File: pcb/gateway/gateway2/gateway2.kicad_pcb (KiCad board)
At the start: 4 copper layers, 77 x 47 mm, 119 parts, among them J1 Conn_ARM_JTAG_SWD_10, J10 Conn_01x07, J2 RJ45_Kycon_G7LX-A88S7-BP-GY, J8 Conn_01x07, J9 Conn_01x07, P1 USB_C_Plug_USB2.0, SW1 RST, SW2 BOOT, U1 RP2354B, U10 74AHC125, U2 W6300-Q, U3 RT6150AGQW, U8 74AHC125, U9 74AHC125, Y1 ABM8-272-T3, Y2 25MHz

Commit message: WIP.
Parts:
- removed C43, C44: 100n, Capacitor_SMD:C_0603_1608Metric
- removed CP6, CP7: C_Array_4x0612, AVX_Capacitor_Array:C_Array_4x0612
- removed J10, J9: Conn_01x07, Connector_JST:JST_GH_BM07B-GHS-TBT_1x07-1MP_P1.25mm_Vertical
- removed JP11, JP13: SolderJumper_2_Open, Jumper:SolderJumper-2_P1.3mm_Open_RoundedPad1.0x1.5mm
- removed JP12, JP14: SolderJumper_2_Bridged, Jumper:SolderJumper-2_P1.3mm_Bridged_RoundedPad1.0x1.5mm
- removed L6: AOTA-B201610S3R3-101-T, Abracon_AOTA_B201610S:L_0806_2016Metric
- removed R36, R39: 100k, Resistor_SMD:R_0603_1608Metric
- removed R37, R40: 10k, Resistor_SMD:R_0603_1608Metric
- removed RN6, RN7: R_Pack04, Resistor_SMD:R_Array_Concave_4x0603
- removed U10, U9: 74AHC125, Package_DFN_QFN:DHVQFN-14-1EP_2.5x3mm_P0.5mm_EP1x1.5mm
- added L1: L, Inductor_SMD:L_Abracon_AOTA-B201610S, F.Cu at (145.7, 70.2)
- U2: footprint WIZnet_W6300:W6300-Q -> Package_QFP:LQFP-48-1EP_7x7mm_P0.5mm_EP3.6x3.6mm_ThermalVias
- moved R11 108.0 mm to (100.9, 68.7)
- moved R10 104.2 mm to (100.5, 91.2)
- moved C30 94.3 mm to (107.0, 92.8)
- moved L4 92.1 mm to (111.8, 99.2)
- moved C23 91.8 mm to (108.1, 99.2)
- moved C22 88.6 mm to (111.3, 93.8)
- moved C17 87.5 mm to (108.5, 96.2)
- moved R19 86.8 mm to (121.2, 98.8)
- moved R18 86.8 mm to (121.2, 97.0)
- moved R23 84.0 mm to (160.6, 59.0)
- moved R24 81.5 mm to (163.6, 60.4)
- moved R21 80.3 mm to (170.5, 65.7)
- moved R22 78.2 mm to (164.1, 63.3)
- moved R20 76.7 mm to (169.7, 69.1)
- moved R25 76.2 mm to (162.3, 69.3)
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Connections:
- net Net-(P1-D+-PadA6) renamed /USB_D+
- net Net-(P1-D--PadA7) renamed /USB_D-
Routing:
- net +1V1: track 15.0 -> 29.0 mm, vias 3 -> 9
- net /USB_D+: track 0.00 -> 8.34 mm
- net /USB_D-: track 0.00 -> 7.97 mm
- net Net-(U1-VREG_AVDD): track 0.00 -> 5.84 mm
- net Net-(U1-USB_DM): track 4.50 -> 8.23 mm
- net Net-(U1-SWCLK): track 0.00 -> 2.61 mm
- net Net-(U1-SWDIO): track 0.00 -> 1.91 mm
- net GND: track 15.1 -> 14.5 mm, vias 25 -> 26
- net +3V3: track 17.4 -> 17.8 mm, vias 3 -> 4

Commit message: Moving stuff to proper library.
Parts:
- L1: value L -> 3.3µ
- SW1, SW2: footprint Littelfuse_CK_PTS815:SW_SPST_CK_PTS815_Sx250SMTR_LFS -> Button_Switch_SMD:SW_SPST_CK_PTS815_Sx250SMTR_LFS
- U3: footprint Richtek_RT6150:WDFN-10-1EP_3x3mm_P0.5mm_EP1.8x2.5mm -> Package_DFN_QFN:WDFN-10-1EP_3x3mm_P0.5mm_EP1.8x2.5mm
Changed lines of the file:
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@@
 		(tags "capacitor")
 		(property "Reference" "C42"
-			(at 0 -1.43 0)
+			(at -0.05 1.5 0)
 			(layer "F.SilkS")
 			(effects
@@
 		(tags "DHVQFN NoLead")
 		(property "Reference" "U8"
-			(at 0 -2.8 0)
+			(at 2.7 2.2875 0)
 			(layer "F.SilkS")
 			(effects
@@
 			)
 		)
-		(model "${KIPRJMOD}/Models/74AHC125BQ,115.stp"
-			(offset
-				(xyz 0 0 0)
-			)
-			(scale
-				(xyz 1 1 1)
-			)
-			(rotate
-				(xyz -0 -0 -0)
-			)
-		)
 	)
 	(footprint "Resistor_SMD:R_0603_1608Metric"
@@
 		)
 	)
-	(footprint "Littelfuse_CK_PTS815:SW_SPST_CK_PTS815_Sx250SMTR_LFS"
+	(footprint "Button_Switch_SMD:SW_SPST_CK_PTS815_Sx250SMTR_LFS"
 		(layer "F.Cu")
 		(at 148.3 60.55)
@@
 			)
 		)
-		(pad "1" smd rect
+		(pad "1" smd roundrect
 			(at -2.25 -1.075)
 			(size 1 0.7)
 			(layers "F.Cu" "F.Mask" "F.Paste")
+			(roundrect_rratio 0.25)
 			(net "GND")
 			(pinfunction "1_1")
 			(pintype "passive")
 		)
-		(pad "1" smd rect
+		(pad "1" smd roundrect
 			(at 2.25 -1.075)
 			(size 1 0.7)
 			(layers "F.Cu" "F.Mask" "F.Paste")
+			(roundrect_rratio 0.25)
 			(net "GND")
 			(pinfunction "1_1")
@@
 		)
 		(embedded_fonts no)
-		(model "${KIPRJMOD}/Littelfuse_CK_PTS815_KiCad_Library/Littelfuse_CK_PTS815.3dshapes/SW_SPST_CK_PTS815_Sx250SMTR_LFS.step"
+		(model "${KICAD10_3DMODEL_DIR}/Button_Switch_SMD.3dshapes/SW_SPST_CK_PTS815_Sx250SMTR_LFS.step"
 			(offset
 				(xyz 0 0 0)
@@
 			)
 		)
-		(model "${KIPRJMOD}/Models/RJ45_Kycon_G7LX-A88S7-BP-GY_Horizontal.wrl"
-			(offset
-				(xyz 0 0 0)
-			)
-			(scale
-				(xyz 1 1 1)
-			)
-			(rotate
-				(xyz 0 0 0)
-			)
-		)
 	)
-	(footprint "Richtek_RT6150:WDFN-10-1EP_3x3mm_P0.5mm_EP1.8x2.5mm"
+	(footprint "Package_DFN_QFN:WDFN-10-1EP_3x3mm_P0.5mm_EP1.8x2.5mm"
 		(layer "F.Cu")
 		(at 159.025 66.1)
-		(descr "Richtek RT6150AGQW, WDFN-10L 3x3mm P0.5mm, exposed-pad land pattern 1.8x2.5mm; copied from KiCad stock WDFN-10 footprint")
+		(descr "WDFN, 10 Pin (https://www.onsemi.com/pdf/datasheet/nis5420-d.pdf)")
 		(tags "WDFN NoLead")
 		(property "Reference" "U3"
-			(at 3.175 -0.7 0)
+			(at 0 -2.45 0)
 			(layer "F.SilkS")
 			(effects
@@
 			(unit
 				(name "A")
-				(pins "6" "7" "8" "3" "9" "5" "11" "1" "10" "2" "4")
+				(pins "8" "5" "6" "7" "3" "9" "11" "1" "10" "2" "4")
 			)
 		)
@@
 		)
 		(embedded_fonts no)
-		(model "${KIPRJMOD}/Richtek_RT6150_KiCad_Library/Richtek_RT6150.3dshapes/DFN-10-1EP_3x3mm_P0.5mm_EP1.65x2.38mm.step"
+		(model "${KICAD10_3DMODEL_DIR}/Package_DFN_QFN.3dshapes/WDFN-10-1EP_3x3mm_P0.5mm_EP1.8x2.5mm.step"
 			(offset
 				(xyz 0 0 0)
@@
 		)
 		(embedded_fonts no)
-		(model "${KIPRJMOD}/Models/CA064X104M8RACTU.step"
-			(offset
-				(xyz 1.5 0.8 0)
-			)
-			(scale
-				(xyz 1 1 0.8)
-			)
-			(rotate
-				(xyz -0 -0 -90)
-			)
-		)
 	)
 	(footprint "Capacitor_SMD:C_0603_1608Metric"
@@
 			)
 		)
-		(property "Value" "L"
+		(property "Value" "3.3µ"
 			(at 0 1.55 0)
 			(layer "F.Fab")
@@
 		)
 	)
-	(footprint "Littelfuse_CK_PTS815:SW_SPST_CK_PTS815_Sx250SMTR_LFS"
+	(footprint "Button_Switch_SMD:SW_SPST_CK_PTS815_Sx250SMTR_LFS"
 		(layer "F.Cu")
 		(at 134.475 60.1)
@@
 			)
 		)
-		(pad "1" smd rect
+		(pad "1" smd roundrect
 			(at -2.25 -1.075)
 			(size 1 0.7)
 			(layers "F.Cu" "F.Mask" "F.Paste")
+			(roundrect_rratio 0.25)
 			(net "GND")
 			(pinfunction "1_1")
 			(pintype "passive")
 		)
-		(pad "1" smd rect
+		(pad "1" smd roundrect
 			(at 2.25 -1.075)
 			(size 1 0.7)
 			(layers "F.Cu" "F.Mask" "F.Paste")
+			(roundrect_rratio 0.25)
 			(net "GND")
 			(pinfunction "1_1")
@@
 		)
 		(embedded_fonts no)
-		(model "${KIPRJMOD}/Littelfuse_CK_PTS815_KiCad_Library/Littelfuse_CK_PTS815.3dshapes/SW_SPST_CK_PTS815_Sx250SMTR_LFS.step"
+		(model "${KICAD10_3DMODEL_DIR}/Button_Switch_SMD.3dshapes/SW_SPST_CK_PTS815_Sx250SMTR_LFS.step"
 			(offset
 				(xyz 0 0 0)

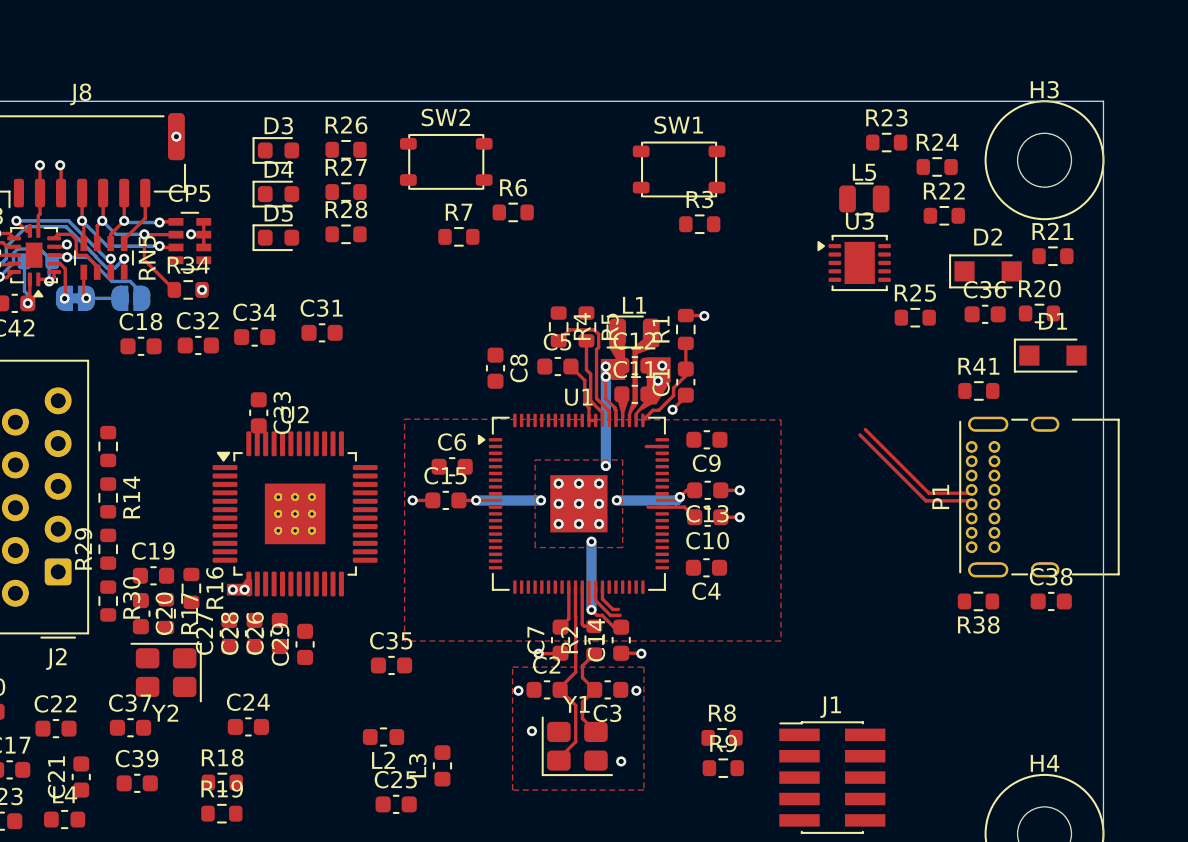
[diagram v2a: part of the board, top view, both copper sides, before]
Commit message: Working on power converter.
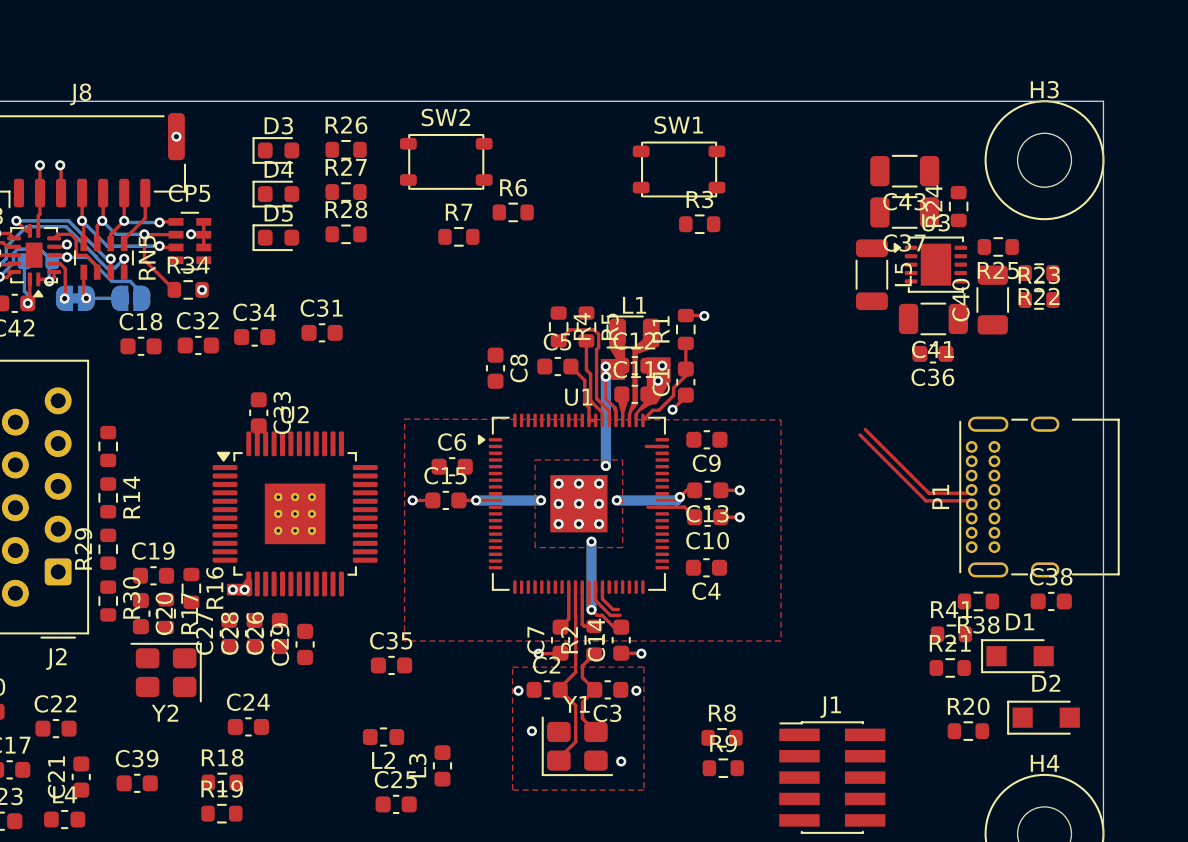
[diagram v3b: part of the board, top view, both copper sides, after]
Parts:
- added C40: 22μ/6.3V, Capacitor_SMD:C_1206_3216Metric, F.Cu at (166.9, 68.3)
- added C41: 22μ/6.3V, Capacitor_SMD:C_1206_3216Metric, F.Cu at (163.4, 69.4)
- added C43: 22μ/6.3V, Capacitor_SMD:C_1206_3216Metric, F.Cu at (161.7, 60.6)
- C37: value 47μ/6.3V -> 22μ/6.3V; footprint Capacitor_SMD:C_0603_1608Metric -> Capacitor_SMD:C_1206_3216Metric
- L5: footprint Abracon_AOTA_B201610S:L_0806_2016Metric -> Inductor_SMD:L_1206_3216Metric
- moved C37 55.2 mm to (161.7, 63.1), turned to 180 degrees
- moved D2 26.7 mm to (170.1, 93.1)
- moved R21 25.2 mm to (164.4, 90.2)
- moved R20 25.2 mm to (165.5, 93.9)
- moved D1 18.0 mm to (168.6, 89.5)
- moved R41 14.5 mm to (164.5, 88.2)
- moved R23 13.0 mm to (169.7, 68.3)
- moved R22 6.57 mm to (169.7, 66.7), turned to 180 degrees
- moved R25 6.47 mm to (167.2, 65.2), turned to 180 degrees
- moved U3 4.53 mm to (163.6, 66.2)
- moved L5 4.52 mm to (159.8, 66.8), turned to -90 degrees
- moved C36 3.89 mm to (163.4, 71.5), turned to 180 degrees
- moved R24 2.67 mm to (164.9, 62.8), turned to 90 degrees

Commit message: Power converter routed.
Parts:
- moved D1 17.9 mm to (160.5, 73.5), turned to -90 degrees
- moved R9 8.81 mm to (148.6, 87.6)
- moved J1 7.29 mm to (159.2, 89.6)
- moved R20 6.96 mm to (164.6, 87.0), turned to -90 degrees
- moved R8 5.57 mm to (148.6, 89.2), turned to 180 degrees
- moved R41 5.06 mm to (169.4, 87.0), turned to 90 degrees
- moved R21 3.63 mm to (166.2, 87.0), turned to -90 degrees
- moved C41 3.62 mm to (162.8, 73.0), turned to 90 degrees
- moved C43 3.56 mm to (164.0, 63.4)
- moved C37 3.54 mm to (164.0, 65.8)
- moved R24 3.48 mm to (167.2, 65.4)
- moved C40 2.68 mm to (167.6, 70.9)
- moved R23 2.68 mm to (170.3, 70.9)
- moved R25 2.68 mm to (167.9, 67.8)
- moved R22 2.68 mm to (170.3, 69.3), turned to 0 degrees
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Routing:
- net /Power/V_USB: track 0.00 -> 22.1 mm, vias 0 -> 1
- net GNDPWR: track 0.00 -> 19.9 mm
- net GND: track 14.5 -> 26.5 mm, vias 26 -> 40
- net Net-(P1-CC2): track 0.00 -> 8.98 mm, vias 0 -> 1
- net Net-(U3-EN): track 0.00 -> 8.32 mm, vias 0 -> 2
- net POWER_SAVE: track 0.00 -> 7.09 mm, vias 0 -> 2
- net Net-(P1-CC1): track 0.00 -> 6.88 mm
- net +3V3: track 17.8 -> 23.2 mm, vias 4 -> 9
- net +5V: track 0.00 -> 4.60 mm
- net Net-(U1-SWCLK): track 2.61 -> 6.49 mm
- net Net-(U1-SWDIO): track 1.91 -> 5.37 mm
- net /USB_D-: track 7.97 -> 11.1 mm
- net /USB_D+: track 8.34 -> 11.4 mm
- net Net-(U3-FB): track 0.00 -> 2.98 mm
- net VBUS_MONITOR: track 0.00 -> 2.31 mm

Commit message: Lookinmg where to place the buttons at.
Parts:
- moved SW2 31.1 mm to (160.0, 77.8)
- moved R7 24.9 mm to (154.6, 80.2)
- moved SW1 24.6 mm to (160.0, 82.2), turned to 180 degrees
- moved R6 22.2 mm to (154.6, 78.4)
- moved R3 21.3 mm to (154.8, 84.4), turned to 180 degrees
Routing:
- net /USB_D+: track 11.4 -> 1.70 mm
- net Net-(U1-RUN): track 0.00 -> 9.29 mm
- net /USB_D-: track 11.1 -> 2.03 mm
- net /Power/V_USB: track 22.1 -> 23.3 mm
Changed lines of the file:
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@@
 	(footprint "Resistor_SMD:R_0603_1608Metric"
 		(layer "F.Cu")
-		(at 138.45 63.1)
+		(at 154.6 78.4)
 		(descr "Resistor SMD 0603 (1608 Metric), square (rectangular) end terminal, IPC-7351 nominal, (Body size source: IPC-SM-782 page 72, https://www.pcb-3d.com/wordpress/wp-content/uploads/ipc-sm-782a_amendment_1_and_2.pdf)")
 		(tags "resistor")
@@
 	(footprint "Button_Switch_SMD:SW_SPST_CK_PTS815_Sx250SMTR_LFS"
 		(layer "F.Cu")
-		(at 148.3 60.55)
+		(at 160 82.2 180)
 		(descr "C&K / Littelfuse PTS815 series microminiature SMT top-actuated tactile switch, 4.2 x 3.2 mm, 2.5 mm height")
 		(tags "C&K Littelfuse PTS815 tactile SPST NO switch")
@@
 		(duplicate_pad_numbers_are_jumpers no)
 		(fp_line
-			(start -2.2 -1.6)
-			(end -2.2 -1.45)
+			(start 2.2 1.45)
+			(end 2.2 1.6)
 			(stroke
 				(width 0.12)
@@
 		)
 		(fp_line
-			(start -2.2 -0.7)
-			(end -2.2 0.7)
+			(start 2.2 -0.7)
+			(end 2.2 0.7)
 			(stroke
 				(width 0.12)
@@
 		)
 		(fp_line
-			(start -2.2 1.45)
-			(end -2.2 1.6)
+			(start 2.2 -1.6)
+			(end 2.2 -1.45)
 			(stroke
 				(width 0.12)
@@
 		)
 		(fp_line
-			(start -2.1 -1.6)
-			(end 2.1 -1.6)
+			(start -2.1 1.6)
+			(end 2.1 1.6)
 			(stroke
 				(width 0.12)
@@
 		)
 		(fp_line
-			(start -2.1 1.6)
-			(end 2.1 1.6)
+			(start -2.1 -1.6)
+			(end 2.1 -1.6)
 			(stroke
 				(width 0.12)
@@
 		)
 		(fp_line
-			(start 2.2 -1.6)
-			(end 2.2 -1.45)
+			(start -2.2 1.45)
+			(end -2.2 1.6)
 			(stroke
 				(width 0.12)
@@
 		)
 		(fp_line
-			(start 2.2 -0.7)
-			(end 2.2 0.7)
+			(start -2.2 -0.7)
+			(end -2.2 0.7)
 			(stroke
 				(width 0.12)
@@
 		)
 		(fp_line
-			(start 2.2 1.45)
-			(end 2.2 1.6)
+			(start -2.2 -1.6)
+			(end -2.2 -1.45)
 			(stroke
 				(width 0.12)
@@
 		)
 		(pad "1" smd roundrect
-			(at -2.25 -1.075)
+			(at -2.25 -1.075 180)
 			(size 1 0.7)
 			(layers "F.Cu" "F.Mask" "F.Paste")
@@
 		)
 		(pad "1" smd roundrect
-			(at 2.25 -1.075)
+			(at 2.25 -1.075 180)
 			(size 1 0.7)
 			(layers "F.Cu" "F.Mask" "F.Paste")
@@
 		)
 		(pad "2" smd roundrect
-			(at -2.25 1.075)
+			(at -2.25 1.075 180)
 			(size 1 0.7)
 			(layers "F.Cu" "F.Mask" "F.Paste")
@@
 		)
 		(pad "2" smd roundrect
-			(at 2.25 1.075)
+			(at 2.25 1.075 180)
 			(size 1 0.7)
 			(layers "F.Cu" "F.Mask" "F.Paste")
@@
 	(footprint "Resistor_SMD:R_0603_1608Metric"
 		(layer "F.Cu")
-		(at 149.525 63.8)
+		(at 154.825 84.4 180)
 		(descr "Resistor SMD 0603 (1608 Metric), square (rectangular) end terminal, IPC-7351 nominal, (Body size source: IPC-SM-782 page 72, https://www.pcb-3d.com/wordpress/wp-content/uploads/ipc-sm-782a_amendment_1_and_2.pdf)")
 		(tags "resistor")
@@
 		(duplicate_pad_numbers_are_jumpers no)
 		(fp_line
-			(start -0.237258 -0.5225)
-			(end 0.237258 -0.5225)
+			(start -0.237258 0.5225)
+			(end 0.237258 0.5225)
 			(stroke
 				(width 0.12)
@@
 		)
 		(fp_line
-			(start -0.237258 0.5225)
-			(end 0.237258 0.5225)
+			(start -0.237258 -0.5225)
+			(end 0.237258 -0.5225)
 			(stroke
 				(width 0.12)
@@
 		)
 		(pad "1" smd roundrect
-			(at -0.825 0)
+			(at -0.825 0 180)
 			(size 0.8 0.95)
 			(layers "F.Cu" "F.Mask" "F.Paste")
@@
 		)
 		(pad "2" smd roundrect
-			(at 0.825 0)
+			(at 0.825 0 180)
 			(size 0.8 0.95)
 			(layers "F.Cu" "F.Mask" "F.Paste")
@@
 	(footprint "Resistor_SMD:R_0603_1608Metric"
 		(layer "F.Cu")
-		(at 135.225 64.55)
+		(at 154.575 80.2)
 		(descr "Resistor SMD 0603 (1608 Metric), square (rectangular) end terminal, IPC-7351 nominal, (Body size source: IPC-SM-782 page 72, https://www.pcb-3d.com/wordpress/wp-content/uploads/ipc-sm-782a_amendment_1_and_2.pdf)")
 		(tags "resistor")
@@
 	(footprint "Button_Switch_SMD:SW_SPST_CK_PTS815_Sx250SMTR_LFS"
 		(layer "F.Cu")
-		(at 134.475 60.1)
+		(at 160 77.8)
 		(descr "C&K / Littelfuse PTS815 series microminiature SMT top-actuated tactile switch, 4.2 x 3.2 mm, 2.5 mm height")
 		(tags "C&K Littelfuse PTS815 tactile SPST NO switch")
@@
 	)
 	(segment
+		(start 144.15 85.960052)
+		(end 144.514948 86.325)
+		(width 0.2)
+		(layer "F.Cu")
+		(net "Net-(U1-RUN)")
+	)
+	(segment
+		(start 144.15 85.35)
+		(end 144.15 85.960052)
+		(width 0.2)
+		(layer "F.Cu")
+		(net "Net-(U1-RUN)")
+	)
+	(segment
+		(start 144.514948 86.325)
+		(end 152.675 86.325)
+		(width 0.2)
+		(layer "F.Cu")
+		(net "Net-(U1-RUN)")
+	)
+	(segment
 		(start 110.25 67.075)
 		(end 110.775 67.075)
@@
 	)
 	(segment
-		(start 165.475001 79.774999)
-		(end 160.774999 79.774999)
-		(width 0.2)
-		(layer "F.Cu")
-		(net "/USB_D-")
-	)
-	(segment
 		(start 159.390901 76.022703)
 		(end 159.359099 75.990901)
@@
 	)
 	(segment
-		(start 160.774999 79.774999)
-		(end 159.390901 78.390901)
-		(width 0.2)
-		(layer "F.Cu")
-		(net "/USB_D-")
-	)
-	(segment
-		(start 159.390901 78.390901)
-		(end 159.390901 76.022703)
-		(width 0.2)
-		(layer "F.Cu")
-		(net "/USB_D-")
-	)
-	(segment
 		(start 165.675 79.575)
 		(end 165.475001 79.774999)
@@
 	)
 	(segment
+		(start 160.475 76.9)
+		(end 161.45 77.875)
+		(width 0.7)
+		(layer "F.Cu")
+		(net "/Power/V_USB")
+	)
+	(segment
 		(start 165.675 82.125)
 		(end 167.025 82.125)
@@
 	)
 	(segment
-		(start 169.4 78.8)
-		(end 168.475 77.875)
+		(start 161.45 77.875)
+		(end 165.675 77.875)
 		(width 0.7)
 		(layer "F.Cu")
@@
 	)
 	(segment
-		(start 167.025 82.125)
-		(end 168.675 82.125)
+		(start 169.4 78.8)
+		(end 168.475 77.875)
 		(width 0.7)
 		(layer "F.Cu")
@@
 	(segment
 		(start 160.475 74.925)
-		(end 163.425 77.875)
+		(end 160.475 76.9)
 		(width 0.7)
 		(layer "F.Cu")
@@
 	)
 	(segment
-		(start 163.425 77.875)
-		(end 165.675 77.875)
+		(start 167.025 82.125)
+		(end 168.675 82.125)
 		(width 0.7)
 		(layer "F.Cu")
@@
 	)
 	(segment
-		(start 165.475001 80.225001)
-		(end 160.625001 80.225001)
-		(width 0.2)
-		(layer "F.Cu")
-		(net "/USB_D+")
-	)
-	(segment
-		(start 165.675 80.425)
-		(end 165.475001 80.225001)
-		(width 0.2)
-		(layer "F.Cu")
-		(net "/USB_D+")
-	)
-	(segment
-		(start 159.040901 78.640901)
-		(end 159.040901 76.309099)
-		(width 0.2)
-		(layer "F.Cu")
-		(net "/USB_D+")
-	)
-	(segment
 		(start 166.175 80.425)
 		(end 167.025 79.575)
 		(width 0.2)
 		(layer "F.Cu")
-		(net "/USB_D+")
-	)
-	(segment
-		(start 160.625001 80.225001)
-		(end 159.040901 78.640901)
-		(width 0.2)
-		(layer "F.Cu")

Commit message: Trying to unpack wiznet.
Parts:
- moved C22 25.7 mm to (130.8, 77.0), turned to 180 degrees
- moved C23 18.2 mm to (117.8, 83.9)
- moved C21 17.3 mm to (128.3, 88.9)
- moved C30 16.2 mm to (117.8, 80.7)
- moved L3 15.8 mm to (118.7, 93.2), turned to 0 degrees
- moved C35 15.5 mm to (117.8, 82.3)
- moved L4 13.5 mm to (122.9, 91.4), turned to 180 degrees
- moved C31 12.8 mm to (132.5, 81.8), turned to 180 degrees
- moved R16 10.6 mm to (113.9, 94.5)
- moved C34 8.77 mm to (117.8, 77.5)
- moved C32 8.31 mm to (117.9, 79.1)
- moved C19 7.63 mm to (113.3, 91.3)
- moved C28 2.74 mm to (120.5, 89.0)
- moved C33 1.61 mm to (123.2, 73.4)
- moved C26 1.27 mm to (123.7, 89.0)
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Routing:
- net 3V3A: track 0.00 -> 15.0 mm, vias 0 -> 2
- net 1V2D: track 0.00 -> 14.4 mm
- net +3V3: track 23.2 -> 29.4 mm, vias 9 -> 11
- net GND: track 26.5 -> 31.9 mm, vias 40 -> 45
- added copper zone on F.Cu, net 1V2D

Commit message: Fighting ethernet rounting.
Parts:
- moved C25 23.5 mm to (117.8, 79.1)
- moved R30 9.72 mm to (114.4, 76.5), turned to 90 degrees
- moved R14 8.05 mm to (114.4, 88.1)
- moved R15 7.60 mm to (114.4, 84.6)
- moved R29 3.15 mm to (114.4, 80.0), turned to -90 degrees
- moved C32 2.61 mm to (117.7, 76.5)
- moved C34 1.10 mm to (117.8, 76.4)
- moved C30 0.50 mm to (117.8, 81.2)
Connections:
- net Net-(J2-RD+) renamed /WizNet/ETH_TD_P
- net Net-(J2-RD-) renamed /WizNet/ETH_TD_N
- net Net-(J2-TD+) renamed /WizNet/ETH_RD_N
- net Net-(J2-TD-) renamed /WizNet/ETH_RD_P
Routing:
- net /WizNet/ETH_RD_P: track 0.00 -> 25.7 mm
- net /WizNet/ETH_RD_N: track 0.00 -> 25.6 mm
- net /WizNet/ETH_TD_N: track 0.00 -> 25.3 mm
- net /WizNet/ETH_TD_P: track 0.00 -> 25.2 mm
- net 3V3A: track 15.0 -> 10.6 mm, vias 2 -> 1
- net GND: track 31.9 -> 29.8 mm
